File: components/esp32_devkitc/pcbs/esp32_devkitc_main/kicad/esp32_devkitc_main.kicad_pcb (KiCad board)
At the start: 2 copper layers, 65 x 56 mm, 29 parts, among them J1 Conn_02x05_Odd_Even, J2 Conn_02x04_Odd_Even, J3 Conn_01x03_Male, J4 Conn_01x02, P1 Conn_02x20_Odd_Even, U1 ESP32-DEVKITC-32D

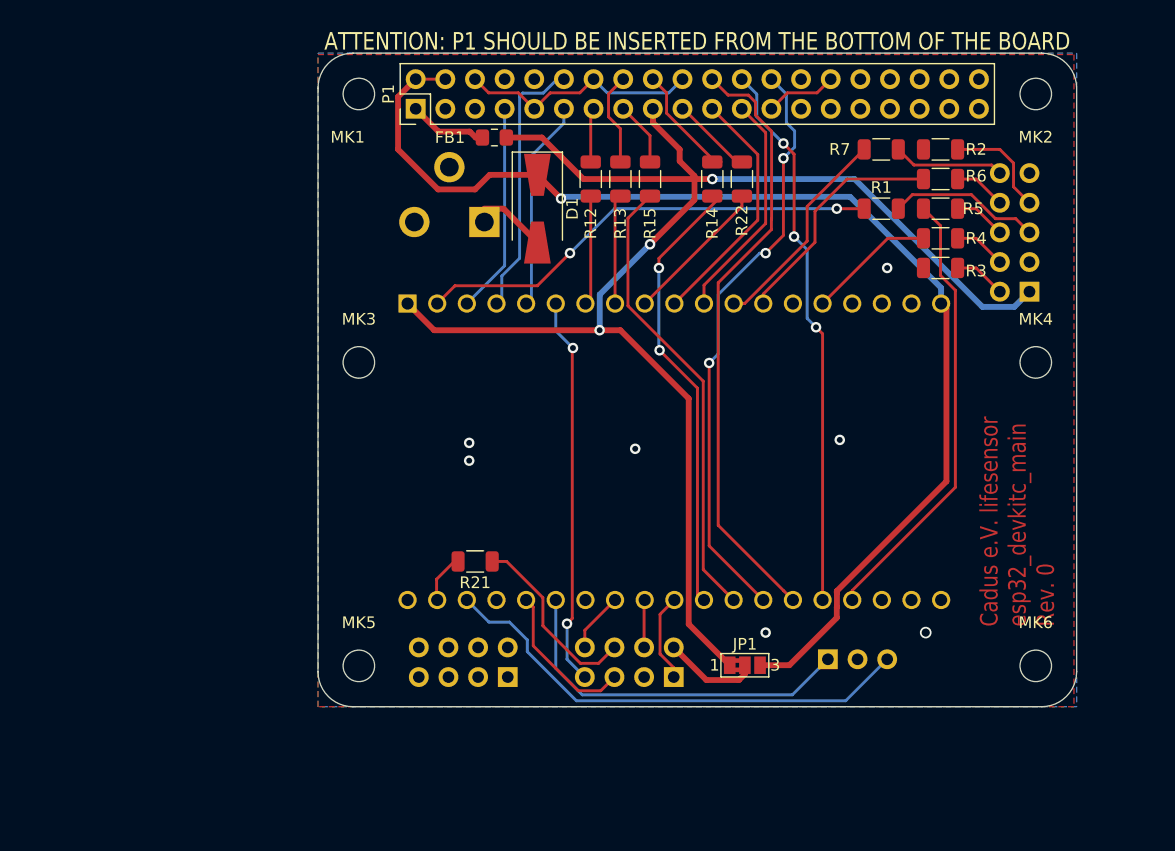
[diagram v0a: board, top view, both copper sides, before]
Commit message: adds gpio expander, WIP
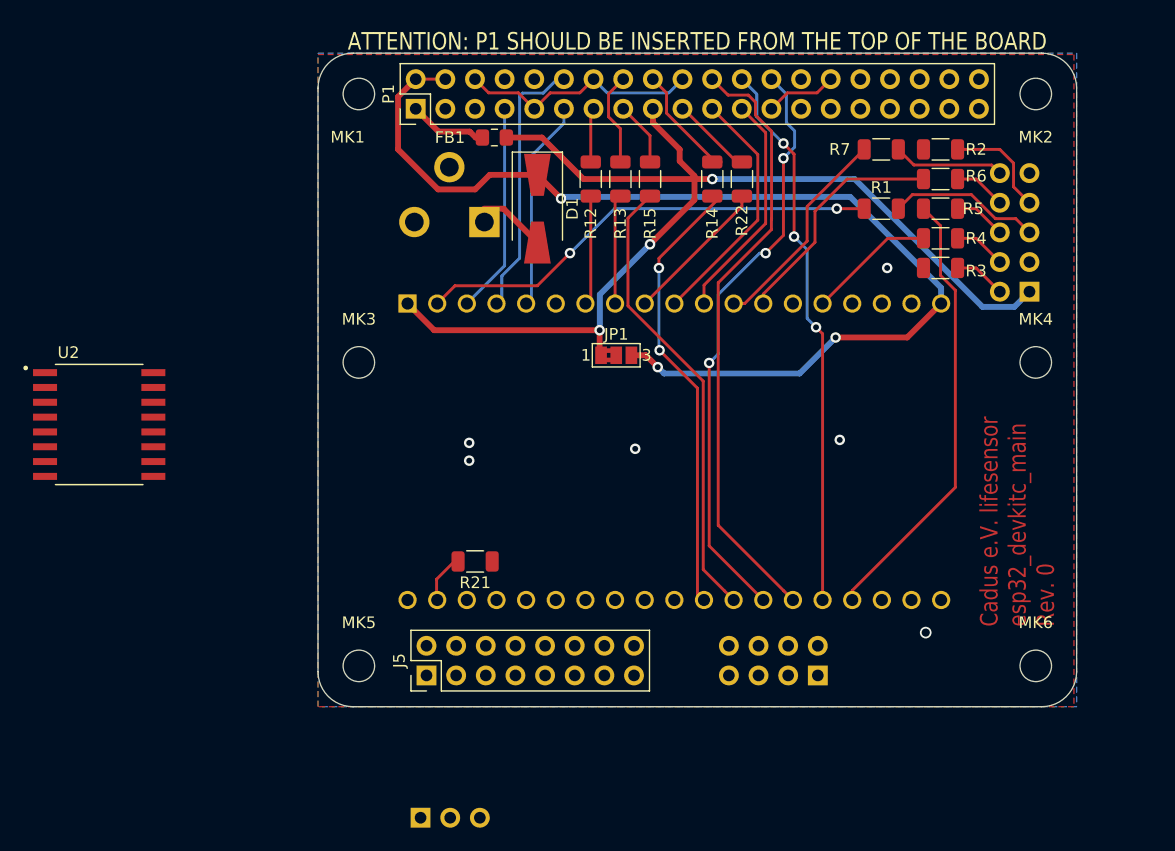
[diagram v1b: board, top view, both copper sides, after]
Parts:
- removed the J2 at (216.3, 147.5)
- removed the J2 at (230.5, 147.5)
- added J2: Conn_02x04_Odd_Even, Connector_PinHeader_2.54mm:PinHeader_2x04_P2.54mm_Vertical, B.Cu at (242.8, 147.3)
- added J5: Button/LED Connector, Connector_PinHeader_2.54mm:PinHeader_2x08_P2.54mm_Vertical, F.Cu at (209.3, 147.3)
- added U2: PCF8574ADWR, SOIC127P1030X265-16N, F.Cu at (181.3, 125.8)
- J4: value Conn_01x02 -> CUI_PJ-102AH_Horizontal
- moved J3 37.4 mm to (208.8, 159.5)
- moved JP1 28.8 mm to (225.6, 119.9)
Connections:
- U1 pad 7: Net-(R12-Pad1) -> /GPIOEXP_INT
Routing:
- net /PROC_SCL: track 41.7 -> 0.00 mm
- net /DISP_INT_TOUCH: track 33.5 -> 0.00 mm, vias 2 -> 0
- net /SENS_3V3_DIG: track 127.0 -> 94.8 mm
- net /PROC_SDA: track 31.4 -> 0.00 mm
- net /DISP_MOSI: track 16.1 -> 0.00 mm
- net /DISP_CS_TOUCH: track 13.2 -> 0.00 mm
- net /SENS_5V_ANA: track 102.4 -> 92.8 mm, vias 1 -> 3
- net Net-(J2-Pad2): track 8.22 -> 0.00 mm
- net /DISP_CS_DISP: track 7.60 -> 0.00 mm
- net /DISP_MISO: track 5.14 -> 0.00 mm
- net /DISP_SCLK: track 4.09 -> 0.00 mm
- net GND: vias 7 -> 6
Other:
- board text added: "ATTENTION: P1 SHOULD BE INSERTED FROM THE TOP OF THE BOARD"
- board text removed: "ATTENTION: P1 SHOULD BE INSERTED FROM THE BOTTOM OF THE BOARD"

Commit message: updates 5V jack, adds jumpers for I2C GPIO Expander Adress, updates pinout, updates docs
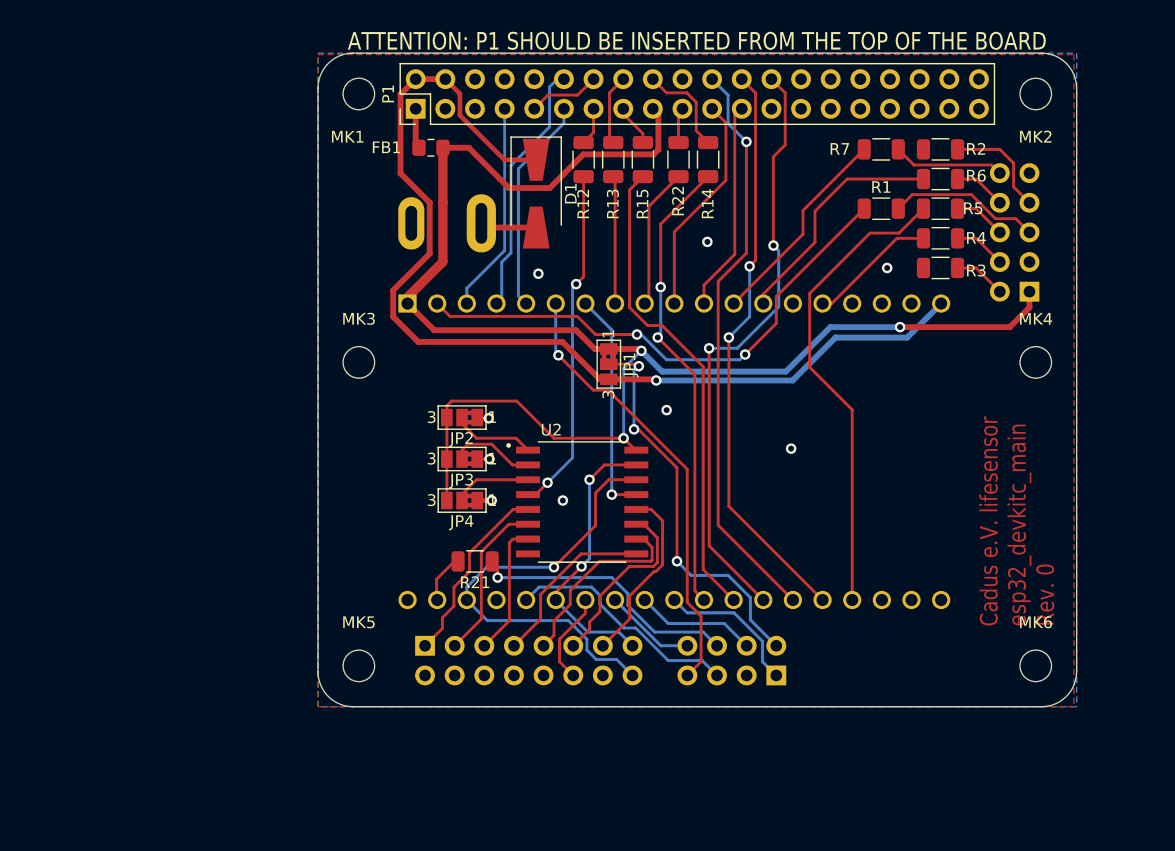
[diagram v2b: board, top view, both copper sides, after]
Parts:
- removed J5: Button/LED Connector, Connector_PinHeader_2.54mm:PinHeader_2x08_P2.54mm_Vertical
- added JP2: Jumper_NC_Dual, Jumper:SolderJumper-3_P1.3mm_Bridged2Bar12_Pad1.0x1.5mm_NumberLabels, F.Cu at (212.3, 125.2)
- added JP3: Jumper_NC_Dual, Jumper:SolderJumper-3_P1.3mm_Bridged2Bar12_Pad1.0x1.5mm_NumberLabels, F.Cu at (212.3, 128.8)
- added JP4: Jumper_NC_Dual, Jumper:SolderJumper-3_P1.3mm_Bridged2Bar12_Pad1.0x1.5mm_NumberLabels, F.Cu at (212.3, 132.3)
- J3: value Conn_01x03_Male -> Button/LED/I2C Connector; footprint Connector_PinHeader_2.54mm:PinHeader_1x03_P2.54mm_Vertical -> Connector_PinHeader_2.54mm:PinHeader_2x08_P2.54mm_Vertical
- J4: footprint Connector_BarrelJack:BarrelJack_CUI_PJ-102AH_Horizontal -> lib_footprint:CUI_PJ-037B
- moved U2 41.9 mm to (222.6, 132.5)
- moved J3 14.7 mm to (209.2, 144.8)
- moved R22 5.68 mm to (230.9, 103.1)
- moved FB1 5.51 mm to (209.7, 102.1)
- moved J2 3.56 mm to (239.3, 147.3)
- moved R15 1.77 mm to (227.8, 103.1)
- moved R12 1.77 mm to (222.8, 103.1)
- moved R13 1.77 mm to (225.3, 103.1)
- moved R14 1.70 mm to (233.4, 103.1)
- moved D1 1.29 mm to (218.7, 106.0)
- moved JP1 0.99 mm to (224.9, 120.7), turned to 270 degrees
- moved J4 0.28 mm to (214.0, 108.6), turned to 180 degrees
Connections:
- J3 pad 1: /PROC_SDA -> /EXPGPIO1
- J3 pad 3: /PROC_SCL -> /EXPGPIO2
- U2 pad 1: GND -> Net-(JP2-Pad2)
- U2 pad 10: /GPIO5 -> /EXPGPIO5
- U2 pad 11: /GPIO6 -> /EXPGPIO6
- U2 pad 12: /GPIO7 -> /EXPGPIO7
- U2 pad 2: GND -> Net-(JP3-Pad2)
- U2 pad 3: GND -> Net-(JP4-Pad2)
- U2 pad 5: /GPIO1 -> /EXPGPIO1
- U2 pad 6: /GPIO2 -> /EXPGPIO2
- U2 pad 7: /GPIO3 -> /EXPGPIO3
- U2 pad 9: /GPIO4 -> /EXPGPIO4
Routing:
- net /PROC_SCL: track 0.00 -> 38.5 mm, vias 0 -> 1
- net /SENS_3V3_DIG: track 94.8 -> 133.3 mm
- net /DISP_INT_TOUCH: track 0.00 -> 38.3 mm, vias 0 -> 1
- net Net-(J2-Pad2): track 0.00 -> 33.9 mm, vias 0 -> 3
- net /PROC_SDA: track 0.00 -> 24.4 mm, vias 0 -> 2
- net /DISP_MOSI: track 0.00 -> 23.4 mm, vias 0 -> 1
- net /DISP_CS_TOUCH: track 0.00 -> 20.4 mm
- net Net-(R12-Pad1): track 9.39 -> 29.6 mm, vias 0 -> 2
- net /GPIOEXP_INT: track 0.00 -> 19.4 mm, vias 0 -> 1
- net /EXPGPIO5: track 0.00 -> 16.5 mm
- net /EXPGPIO1: track 0.00 -> 16.1 mm
- net /EXPGPIO6: track 0.00 -> 15.7 mm
- net /EXPGPIO7: track 0.00 -> 15.6 mm
- net /EXPGPIO4: track 0.00 -> 15.0 mm
- net /EXPGPIO2: track 0.00 -> 14.0 mm
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
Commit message: improve GND return paths for display SPI signals
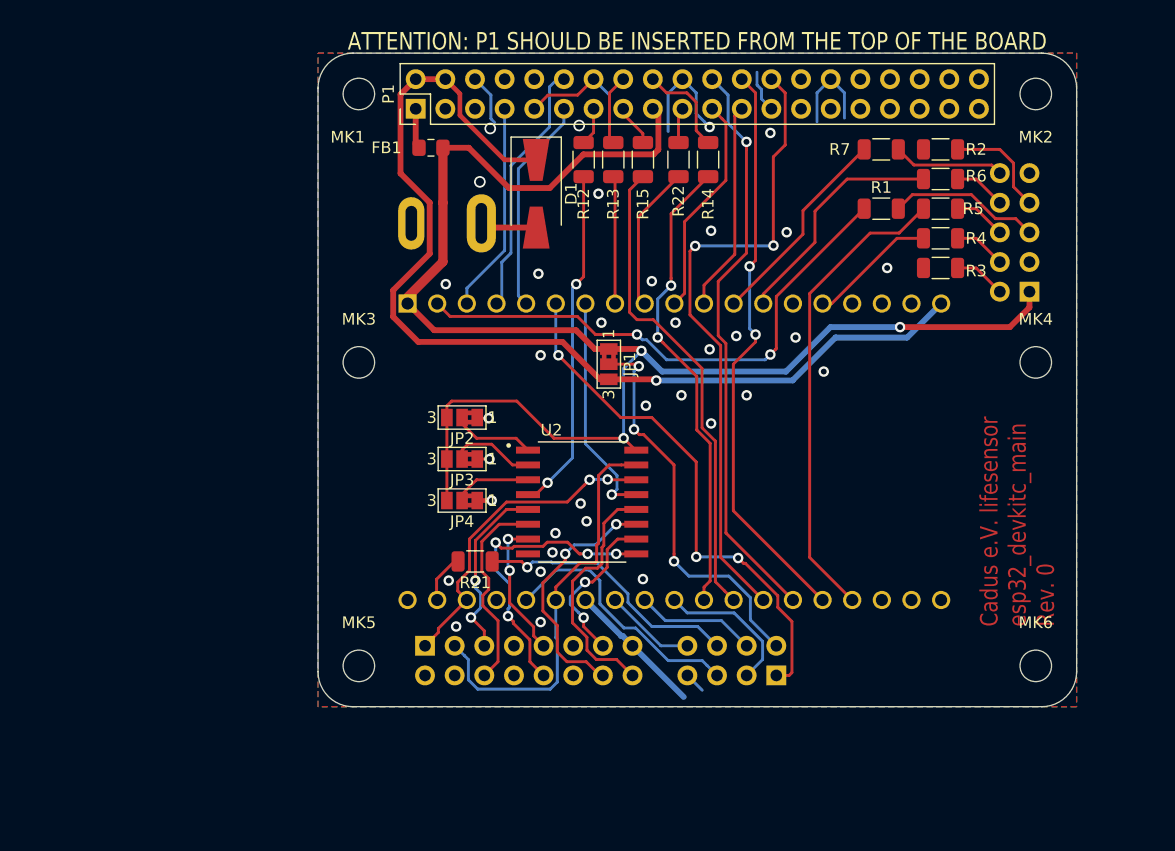
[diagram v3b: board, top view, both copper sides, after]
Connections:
- J2 pad 1: /DISP_CS_DISP -> /DISP_INT_TOUCH
- J2 pad 3: GND -> /DISP_CS_DISP
- J2 pad 7: /DISP_INT_TOUCH -> GND
- J3 pad 1: /EXPGPIO1 -> /PROC_SCL
- J3 pad 10: GND -> /EXPGPIO4
- J3 pad 11: /EXPGPIO6 -> GND
- J3 pad 13: /EXPGPIO7 -> /EXPGPIO5
- J3 pad 14: GND -> /EXPGPIO6
- J3 pad 15: /PROC_SDA -> GND
- J3 pad 16: /PROC_SCL -> /EXPGPIO7
- J3 pad 3: /EXPGPIO2 -> /PROC_SDA
- J3 pad 5: /EXPGPIO3 -> /EXPGPIO1
- J3 pad 6: GND -> /EXPGPIO2
- J3 pad 7: /EXPGPIO4 -> GND
- J3 pad 9: /EXPGPIO5 -> /EXPGPIO3
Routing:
- net GND: track 17.3 -> 53.5 mm, vias 9 -> 35
- net /EXPGPIO4: track 15.0 -> 26.1 mm, vias 0 -> 4
- net /PROC_SDA: track 24.4 -> 35.4 mm, vias 2 -> 0
- net /PROC_SCL: track 38.5 -> 27.8 mm, vias 1 -> 2
- net /DISP_INT_TOUCH: track 38.3 -> 45.1 mm, vias 1 -> 3
- net /EXPGPIO6: track 15.7 -> 21.6 mm, vias 0 -> 2
- net /EXPGPIO7: track 15.6 -> 21.2 mm
- net /~SENS_CS_SPO2: track 51.5 -> 55.3 mm
- net /EXPGPIO2: track 14.0 -> 17.5 mm
- net /EXPGPIO5: track 16.5 -> 14.0 mm, vias 0 -> 2
- net /DISP_CS_TOUCH: track 20.4 -> 22.3 mm
- net /JTAG_~TRST: track 45.3 -> 46.6 mm
- net /EXPGPIO3: track 11.4 -> 12.5 mm, vias 0 -> 2
- net /EXPGPIO1: track 16.1 -> 15.6 mm, vias 0 -> 2
